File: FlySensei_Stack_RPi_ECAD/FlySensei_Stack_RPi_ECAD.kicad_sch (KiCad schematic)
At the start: 0 parts

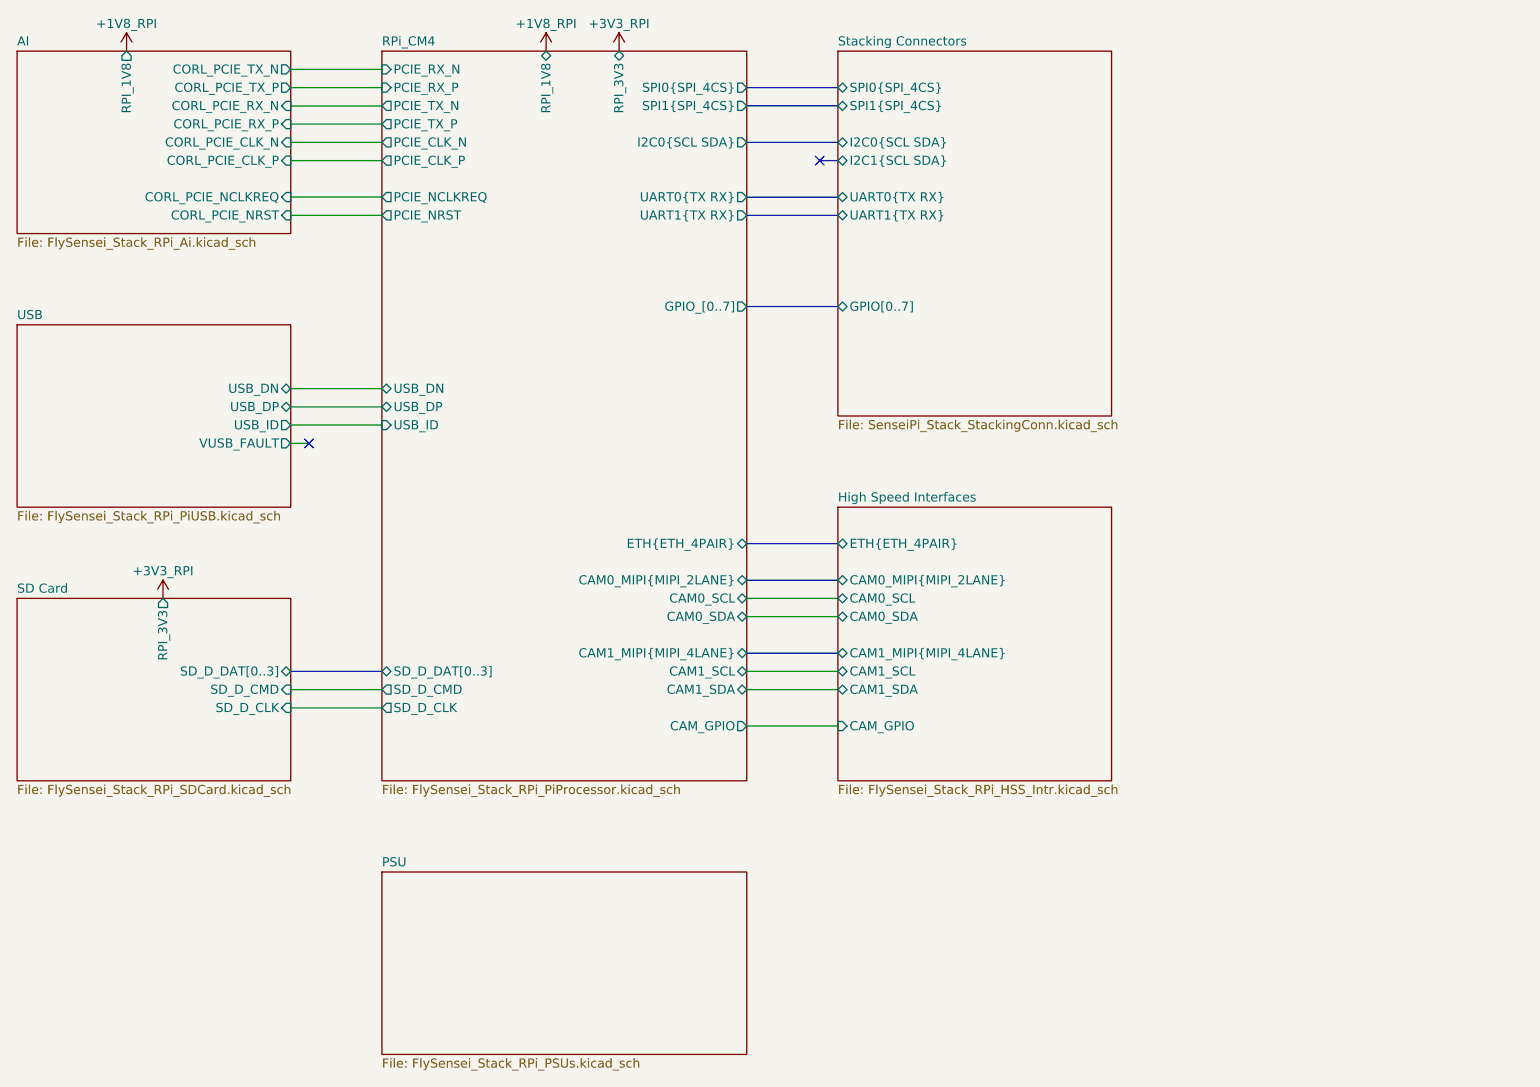
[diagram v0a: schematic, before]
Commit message: PCB Design for the Raspberry PI CM4 Board (V0.1)
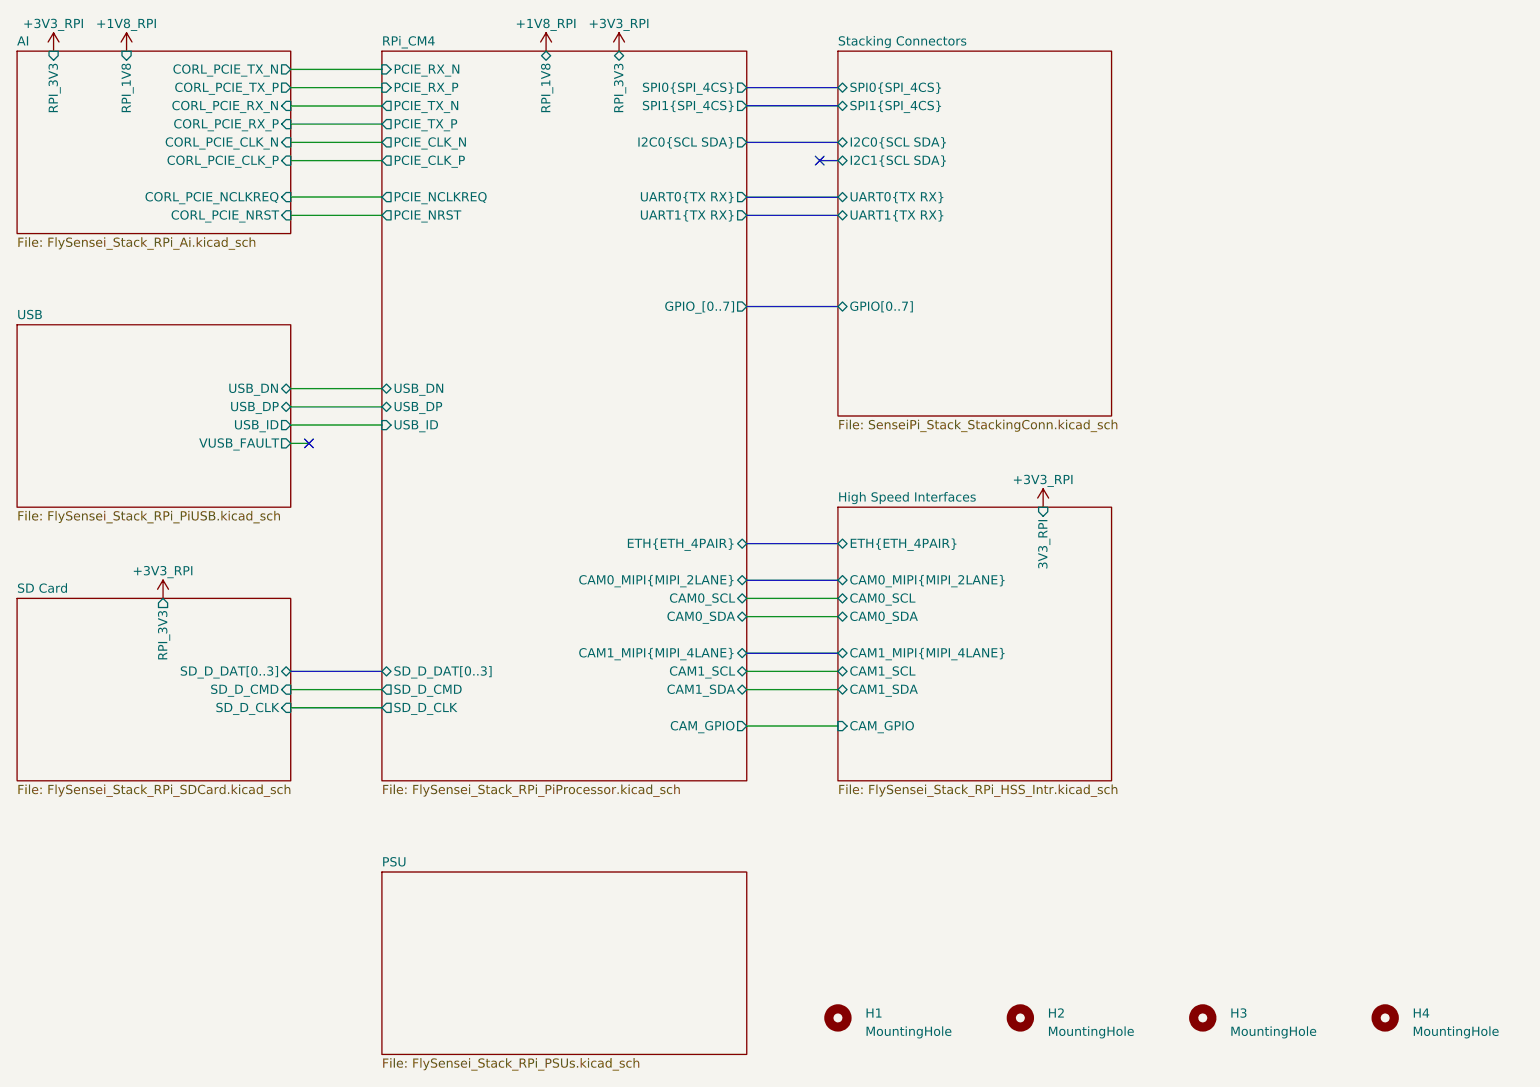
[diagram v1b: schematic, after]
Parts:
- added H1, H2, H3, H4: MountingHole, MountingHole:MountingHole_2.7mm_M2.5_Pad_Via, symbol Mechanical:MountingHole
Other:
- sheet AI ports: added RPI_3V3; removed none
- sheet High Speed Interfaces ports: added 3V3_RPI; removed none

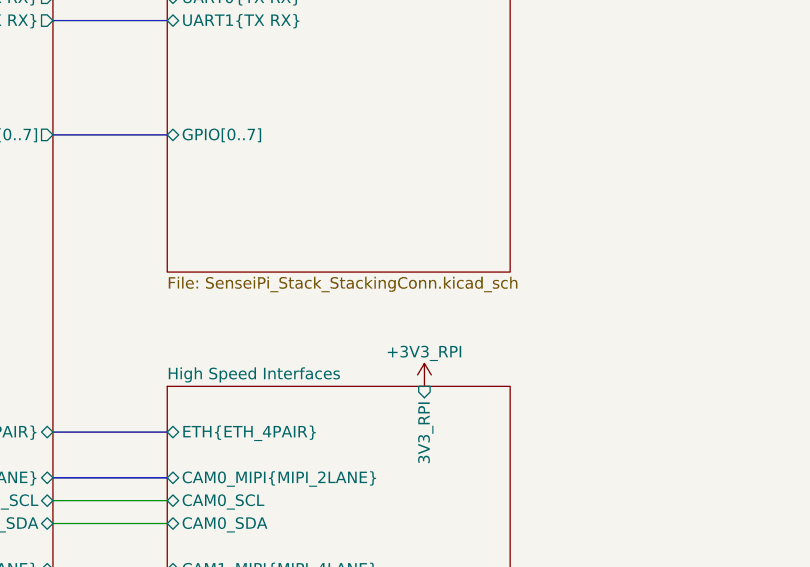
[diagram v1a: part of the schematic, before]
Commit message: Add PCB design for the actuation board
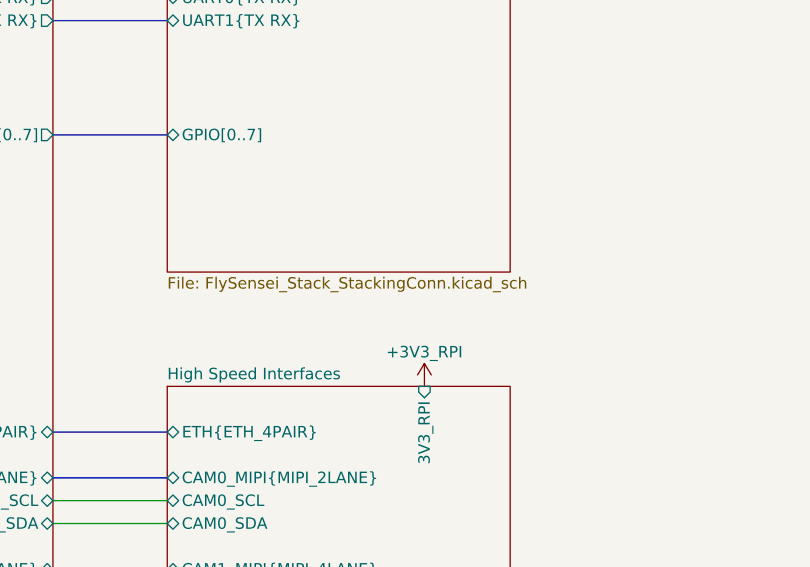
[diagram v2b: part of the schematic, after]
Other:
- sheet Stacking Connectors: file SenseiPi_Stack_StackingConn.kicad_sch -> FlySensei_Stack_StackingConn.kicad_sch
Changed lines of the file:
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@@
       (effects (font (size 1.27 1.27)) (justify left bottom))
     )
-    (property "Sheet file" "SenseiPi_Stack_StackingConn.kicad_sch" (id 1) (at 165.1 76.7087 0)
+    (property "Sheet file" "FlySensei_Stack_StackingConn.kicad_sch" (id 1) (at 165.1 76.7087 0)
       (effects (font (size 1.27 1.27)) (justify left top))
     )
@@
       (reference "#PWR0164") (unit 1) (value "GND") (footprint "")
     )
-    (path "/f22911d6-fd0b-420b-886b-10dcff84029c/54916ec9-af70-477f-b016-b7e6781118dd"
-      (reference "#PWR0165") (unit 1) (value "GND") (footprint "")
-    )
-    (path "/f22911d6-fd0b-420b-886b-10dcff84029c/b5ac56e3-f4c8-45cf-b582-b97ae3ae2b09"
-      (reference "#PWR0166") (unit 1) (value "GND") (footprint "")
-    )
-    (path "/f22911d6-fd0b-420b-886b-10dcff84029c/1ae8c87a-b913-41f6-a1dd-ed54b364fe7f"
-      (reference "#PWR0167") (unit 1) (value "GND") (footprint "")
-    )
-    (path "/f22911d6-fd0b-420b-886b-10dcff84029c/4a4d1cfd-f35f-4065-8365-6bb04e476d94"
-      (reference "#PWR0168") (unit 1) (value "GND") (footprint "")
-    )
-    (path "/f22911d6-fd0b-420b-886b-10dcff84029c/46804df2-3bd5-4575-8af4-f8c1c4312ed3"
-      (reference "#PWR0169") (unit 1) (value "GND") (footprint "")
-    )
-    (path "/f22911d6-fd0b-420b-886b-10dcff84029c/26c4864f-1d8c-4fc8-8cad-51eb7d155f42"
-      (reference "#PWR0170") (unit 1) (value "GND") (footprint "")
-    )
-    (path "/f22911d6-fd0b-420b-886b-10dcff84029c/d1c53479-0edd-4ac6-b4e2-3f03ff22869d"
-      (reference "#PWR0171") (unit 1) (value "+BATT") (footprint "")
-    )
-    (path "/f22911d6-fd0b-420b-886b-10dcff84029c/07826ae3-0f4a-4200-acbc-eebacf289e56"
-      (reference "#PWR0172") (unit 1) (value "+BATT") (footprint "")
-    )
-    (path "/f22911d6-fd0b-420b-886b-10dcff84029c/b2bb658c-dc31-44f6-a275-f49a5b1107e9"
-      (reference "#PWR0173") (unit 1) (value "GND") (footprint "")
-    )
     (path "/1a1df624-ea52-444e-8eb0-2f13ef4aac9c/27a68ec0-b8bb-41a6-87a7-43252d8811fa"
       (reference "#PWR0174") (unit 1) (value "GND") (footprint "")
@@
       (reference "#PWR0189") (unit 1) (value "GND") (footprint "")
     )
+    (path "/f22911d6-fd0b-420b-886b-10dcff84029c/07826ae3-0f4a-4200-acbc-eebacf289e56"
+      (reference "#PWR?") (unit 1) (value "+BATT") (footprint "")
+    )
+    (path "/f22911d6-fd0b-420b-886b-10dcff84029c/1ae8c87a-b913-41f6-a1dd-ed54b364fe7f"
+      (reference "#PWR?") (unit 1) (value "GND") (footprint "")
+    )
     (path "/f22911d6-fd0b-420b-886b-10dcff84029c/208f0a01-713a-4231-a6f0-1c5d1638f8c4"
-      (reference "#PWR0190") (unit 1) (value "GND") (footprint "")
+      (reference "#PWR?") (unit 1) (value "GND") (footprint "")
+    )
+    (path "/f22911d6-fd0b-420b-886b-10dcff84029c/26c4864f-1d8c-4fc8-8cad-51eb7d155f42"
+      (reference "#PWR?") (unit 1) (value "GND") (footprint "")
+    )
+    (path "/f22911d6-fd0b-420b-886b-10dcff84029c/46804df2-3bd5-4575-8af4-f8c1c4312ed3"
+      (reference "#PWR?") (unit 1) (value "GND") (footprint "")
+    )
+    (path "/f22911d6-fd0b-420b-886b-10dcff84029c/4a4d1cfd-f35f-4065-8365-6bb04e476d94"
+      (reference "#PWR?") (unit 1) (value "GND") (footprint "")
+    )
+    (path "/f22911d6-fd0b-420b-886b-10dcff84029c/54916ec9-af70-477f-b016-b7e6781118dd"
+      (reference "#PWR?") (unit 1) (value "GND") (footprint "")
     )
     (path "/f22911d6-fd0b-420b-886b-10dcff84029c/6671dfae-5c2c-4f4b-81fa-bd60b855852c"
-      (reference "#PWR0191") (unit 1) (value "GND") (footprint "")
+      (reference "#PWR?") (unit 1) (value "GND") (footprint "")
+    )
+    (path "/f22911d6-fd0b-420b-886b-10dcff84029c/b2bb658c-dc31-44f6-a275-f49a5b1107e9"
+      (reference "#PWR?") (unit 1) (value "GND") (footprint "")
+    )
+    (path "/f22911d6-fd0b-420b-886b-10dcff84029c/b5ac56e3-f4c8-45cf-b582-b97ae3ae2b09"
+      (reference "#PWR?") (unit 1) (value "GND") (footprint "")
+    )
+    (path "/f22911d6-fd0b-420b-886b-10dcff84029c/d1c53479-0edd-4ac6-b4e2-3f03ff22869d"
+      (reference "#PWR?") (unit 1) (value "+BATT") (footprint "")
     )
     (path "/93e7d8cf-e360-4b54-86be-d58fb9455bdf/f1a7809f-8dd0-490d-9a21-230b15cd185e"
